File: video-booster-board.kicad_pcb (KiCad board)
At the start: 4 copper layers, 36.5 x 41.5 mm, 131 parts, among them IC1 INA180A1IDBVT, J1 0473460001, J10 M20-9990246, J11 MC-HVT1-S04-G, J2 HDMI-PE10-19-LF, J3 HDMI-PE10-19-LF, J6 685119134923_, J9 685119134923_, SW1 1571983-5, U1 PTN3363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

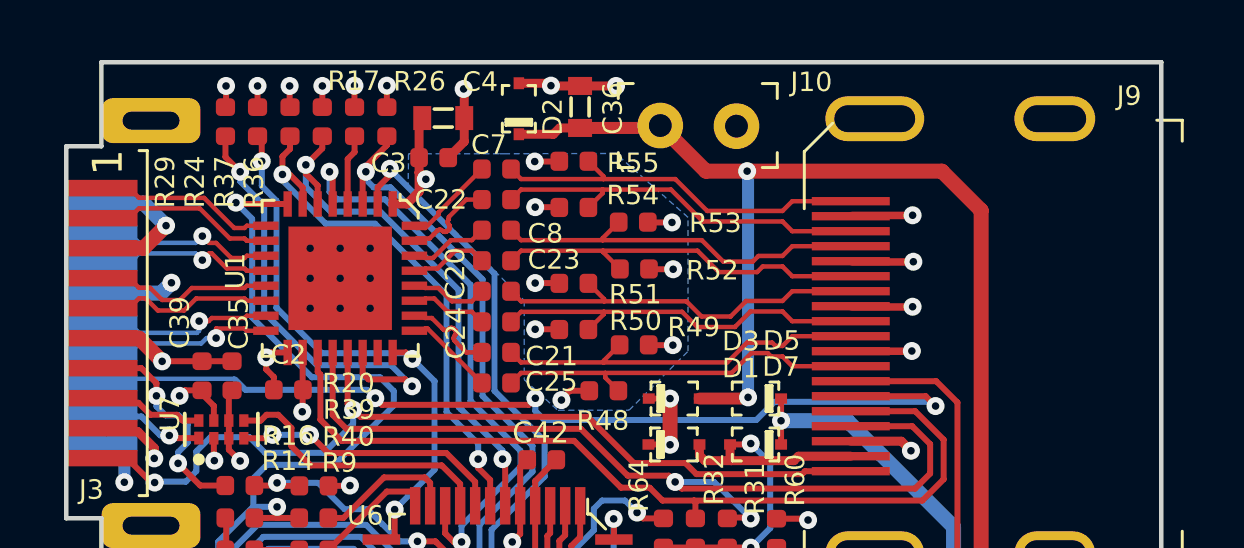
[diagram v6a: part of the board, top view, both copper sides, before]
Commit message: OSHW logo and board name added on PCB
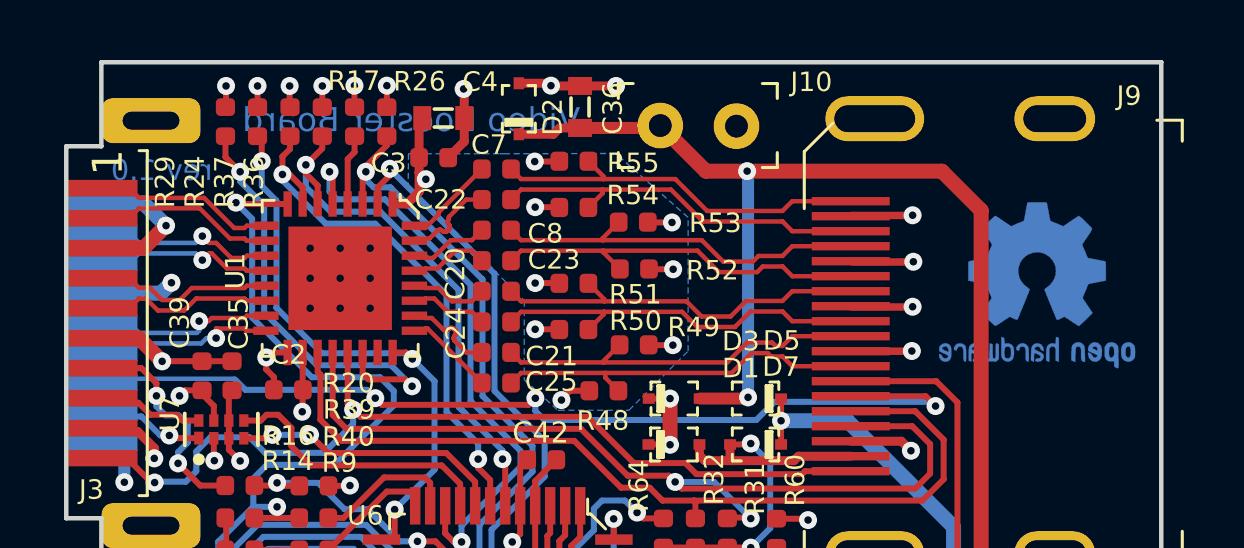
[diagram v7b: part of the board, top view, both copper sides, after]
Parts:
- added N1: oshw_logo, video-booster-board-footprints:OSHW-Logo2_7.3x6mm_Copper_Mask, B.Cu at (145.9, 65.9)
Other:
- board text added: "Video Booster Board"
- board text added: "rev.1.0"

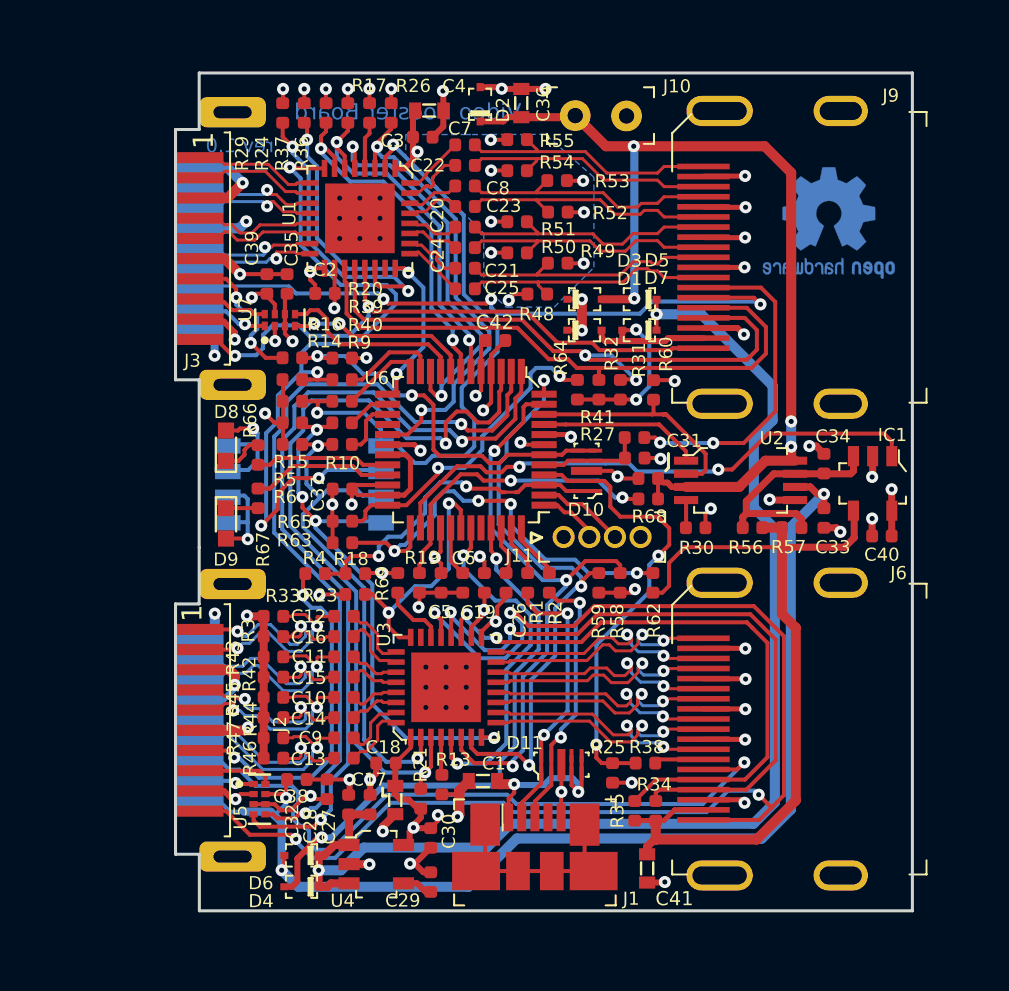
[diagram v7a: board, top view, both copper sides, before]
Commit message: Opsis side HDMI connector type changed. Board shape adjusted, DC jack added
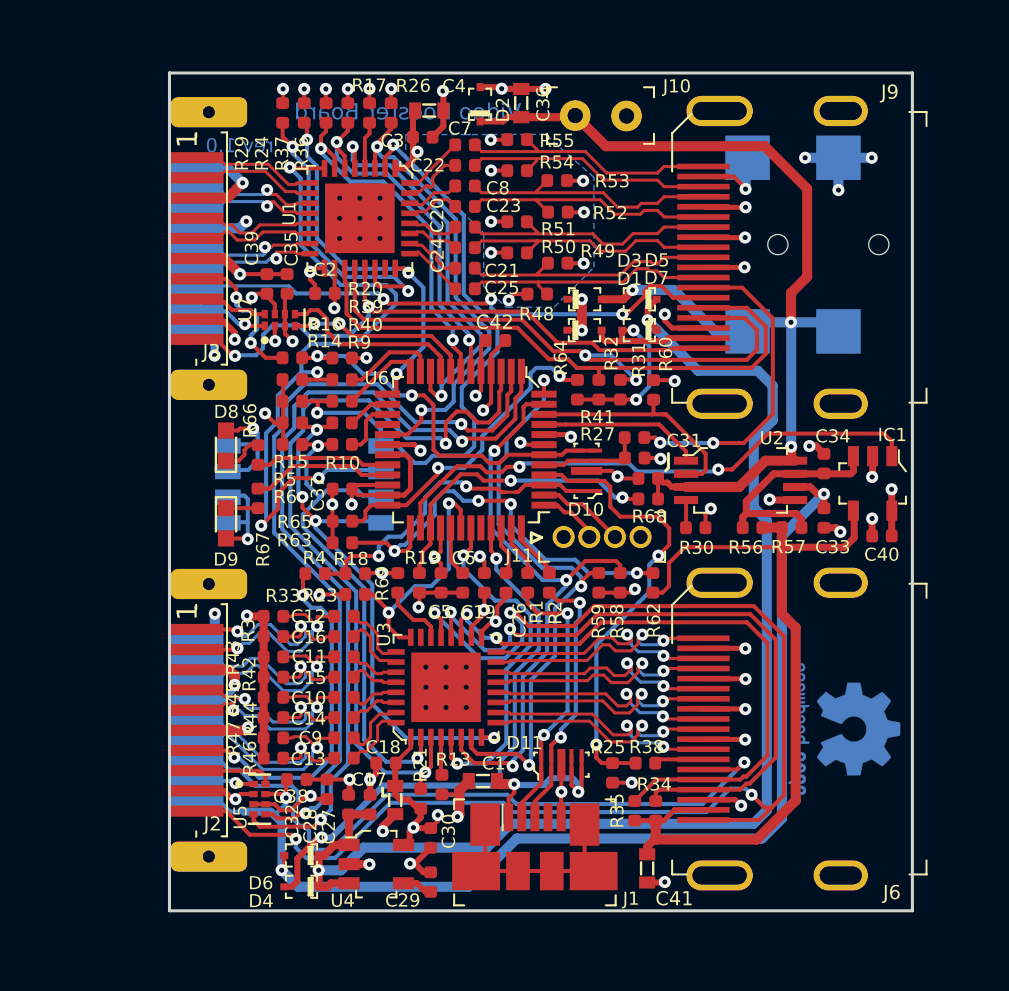
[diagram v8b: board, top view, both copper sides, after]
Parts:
- added J4: 694103107102, video-booster-board-footprints:69410X107102, B.Cu at (149.8, 67.0)
- J2, J3: value HDMI-PE10-19-LF -> CHDMI-AMSS-01-C; footprint video-booster-board-footprints:HDMI-PE10-19-LF -> video-booster-board-footprints:CHDMI-AMSS-01-C
- moved N1 25.1 mm to (146.6, 91.0), turned to 90 degrees
- moved J2 0.15 mm to (114.5, 90.6)
- moved J3 0.15 mm to (114.5, 67.2)
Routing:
- net GND: track 112.8 -> 119.7 mm, vias 51 -> 54
- net /RX_UTILITY: track 32.1 -> 27.0 mm
- net +5VA: track 48.1 -> 52.7 mm, vias 4 -> 3
- net Net-(J9-Pad13): track 16.5 -> 15.9 mm
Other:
- board size 36.5 x 41.5 mm -> 36.8 x 41.5 mm
